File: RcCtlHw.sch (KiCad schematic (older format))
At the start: 27 parts, among them J1 USB_B_Mini, J2 Program, J3 TFT_LCD, SW1 On/Off, U1 TP4056, U2 ESP-M2, U3 ADS1015, U4 Joystick

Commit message: Re-worked USB connector and Joystick to allow oval holes for legs Cleaned up tracks
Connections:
- net at U1.7 (CHRG): now also D1.1 (RA); no longer D1.4 (BA)
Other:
- moved on the sheet: D1
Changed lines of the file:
@@
 F 3 "~" H 4000 2050 50  0001 C CNN
 	1    4000 2100
-	-1   0    0    1
+	-1   0    0    -1
 $EndComp
 Wire Wire Line
@@
 Wire Wire Line
 	3550 2100 3800 2100
-NoConn ~ 3800 2300
 NoConn ~ 2150 1800
 NoConn ~ 2150 1900
@@
 	5250 3750 4750 3750
 Connection ~ 4750 3750
+NoConn ~ 3800 2300
 $EndSCHEMATC

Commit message: More 3D play
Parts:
- D1: footprint LED_THT:LED_D5.0mm-4_RGB -> TrevM:LED_D5.0mm-4_RGB-RIGHT
- J2: footprint Connector_PinHeader_2.54mm:PinHeader_1x06_P2.54mm_Vertical -> TrevM:PinHeader_1x06_P2.54mm_Vertical_bent
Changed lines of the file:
@@
 F 0 "D1" H 4000 1633 50  0000 C CNN
 F 1 "LED_RCGB" H 4000 1724 50  0000 C CNN
-F 2 "LED_THT:LED_D5.0mm-4_RGB" H 4000 2050 50  0001 C CNN
+F 2 "TrevM:LED_D5.0mm-4_RGB-RIGHT" H 4000 2050 50  0001 C CNN
 F 3 "~" H 4000 2050 50  0001 C CNN
 	1    4000 2100
@@
 F 0 "J2" H 8722 1974 50  0000 R CNN
 F 1 "Program" H 8722 1883 50  0000 R CNN
-F 2 "Connector_PinHeader_2.54mm:PinHeader_1x06_P2.54mm_Vertical" H 8750 2000 50  0001 C CNN
+F 2 "TrevM:PinHeader_1x06_P2.54mm_Vertical_bent" H 8750 2000 50  0001 C CNN
 F 3 "~" H 8750 2000 50  0001 C CNN
 	1    8750 2000

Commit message: Added 100n capacitors to ADCs
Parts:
- added C7, C8, C9: 100n, Capacitor_SMD:C_0805_2012Metric, symbol Device:C
- C5, C6: value u1 -> 100n
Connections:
- net GND: now also C7.2, C8.2, C9.2
- net at U3.4 (AIN0), U4.2: now also C7.1
- net at U3.5 (AIN1), U4.5: now also C8.1
- net at R10.1, R9.2, U3.6 (AIN2): now also C9.1
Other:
- moved on the sheet: C5, C6, R8
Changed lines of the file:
@@
 Wire Wire Line
 	7300 5100 7300 5000
-Connection ~ 7650 4300
-Wire Wire Line
-	7650 4600 7650 4300
-Wire Wire Line
-	7650 4900 7650 5000
-Wire Wire Line
-	7300 5000 7650 5000
+Connection ~ 7850 4300
+Wire Wire Line
+	7850 4600 7850 4300
 Wire Wire Line
 	7300 4500 7300 4600
@@
 Text Label 8550 1800 2    39   ~ 0
 3V3
-Connection ~ 7550 1300
+Connection ~ 7650 1300
 Wire Wire Line
 	7950 1800 8550 1800
@@
 	7950 1300 7950 1800
 Wire Wire Line
-	7550 1300 7950 1300
+	7650 1300 7950 1300
 $Comp
 L conn:Conn_01x06_Male J2
@@
 $EndComp
 Wire Wire Line
-	7550 1900 8550 1900
+	7650 1900 8550 1900
 $Comp
 L conn:Conn_01x08_Female J3
@@
 ESP-M2 takes 600 mA max
 Connection ~ 5900 2600
-Wire Wire Line
-	5900 2600 5300 2600
 Connection ~ 8700 3350
 Wire Wire Line
@@
 Wire Wire Line
 	8250 2600 8450 2600
-Wire Wire Line
-	5300 3000 5300 3100
 $Comp
 L TrevM:ADS1015 U3
@@
 $EndComp
 Wire Wire Line
-	7200 4300 7650 4300
+	7200 4300 7850 4300
 $Comp
 L Device:C C6
 U 1 1 60930EB5
-P 7650 4750
-F 0 "C6" H 7765 4796 50  0000 L CNN
-F 1 "u1" H 7765 4705 50  0000 L CNN
-F 2 "Capacitor_SMD:C_0805_2012Metric" H 7688 4600 50  0001 C CNN
-F 3 "~" H 7650 4750 50  0001 C CNN
-	1    7650 4750
+P 7850 4750
+F 0 "C6" H 7850 4850 50  0000 L CNN
+F 1 "100n" H 7850 4650 50  0000 L CNN
+F 2 "Capacitor_SMD:C_0805_2012Metric" H 7888 4600 50  0001 C CNN
+F 3 "~" H 7850 4750 50  0001 C CNN
+	1    7850 4750
 	1    0    0    -1
 $EndComp
@@
 Connection ~ 8250 2600
 $Comp
-L Power:GND #PWR07
-U 1 1 6093378D
-P 5300 3100
-F 0 "#PWR07" H 5300 2850 50  0001 C CNN
-F 1 "GND" H 5305 2927 50  0000 C CNN
-F 2 "" H 5300 3100 50  0001 C CNN
-F 3 "" H 5300 3100 50  0001 C CNN
-	1    5300 3100
-	1    0    0    -1
-$EndComp
-$Comp
 L Power:GND #PWR011
 U 1 1 60932F2B
@@
 L Device:C C5
 U 1 1 6093070F
-P 5300 2850
-F 0 "C5" H 5350 2950 50  0000 L CNN
-F 1 "u1" H 5350 2750 50  0000 L CNN
-F 2 "Capacitor_SMD:C_0805_2012Metric" H 5338 2700 50  0001 C CNN
-F 3 "~" H 5300 2850 50  0001 C CNN
-	1    5300 2850
+P 5900 2850
+F 0 "C5" H 5950 2950 50  0000 L CNN
+F 1 "100n" H 5950 2750 50  0000 L CNN
+F 2 "Capacitor_SMD:C_0805_2012Metric" H 5938 2700 50  0001 C CNN
+F 3 "~" H 5900 2850 50  0001 C CNN
+	1    5900 2850
 	1    0    0    -1
 $EndComp
 Wire Wire Line
 	7350 2500 7550 2500
-Connection ~ 7550 1900
+Connection ~ 7650 1900
 Wire Wire Line
 	7450 2400 8150 2400
@@
 	8150 2400 8150 2000
 Wire Wire Line
-	7550 1900 7350 1900
-Wire Wire Line
-	7550 1700 7550 1900
+	7650 1900 7350 1900
+Wire Wire Line
+	7650 1700 7650 1900
 Connection ~ 7450 1300
 Wire Wire Line
-	7550 1300 7550 1400
-Wire Wire Line
-	7450 1300 7550 1300
+	7650 1300 7650 1400
+Wire Wire Line
+	7450 1300 7650 1300
 $Comp
 L Device:R R8
 U 1 1 6090429E
-P 7550 1550
-F 0 "R8" V 7600 1650 50  0000 L CNN
-F 1 "10K" V 7600 1300 50  0000 L CNN
-F 2 "Resistor_SMD:R_0805_2012Metric" V 7480 1550 50  0001 C CNN
-F 3 "~" H 7550 1550 50  0001 C CNN
-	1    7550 1550
+P 7650 1550
+F 0 "R8" V 7700 1650 50  0000 L CNN
+F 1 "10K" V 7700 1300 50  0000 L CNN
+F 2 "Resistor_SMD:R_0805_2012Metric" V 7580 1550 50  0001 C CNN
+F 3 "~" H 7650 1550 50  0001 C CNN
+	1    7650 1550
 	1    0    0    -1
 $EndComp
@@
 	8350 4000 8350 4300
 Wire Wire Line
-	7650 4300 8350 4300
+	7850 4300 8350 4300
 Connection ~ 8350 4000
 Wire Wire Line
@@
 Connection ~ 6400 4300
 Wire Wire Line
-	7350 2600 7950 2600
+	7350 2600 7450 2600
 NoConn ~ 5950 2300
 Wire Wire Line
@@
 	5700 2100 5950 2100
 Wire Wire Line
-	5300 2700 5300 2600
-Wire Wire Line
-	4850 4200 6300 4200
+	4850 4200 5950 4200
 Wire Wire Line
 	5350 4300 6200 4300
@@
 Connection ~ 4750 3750
 NoConn ~ 3800 2300
+Wire Wire Line
+	7850 5000 7850 4900
+Wire Wire Line
+	7300 5000 7600 5000
+$Comp
+L Device:C C9
+U 1 1 60CFAD69
+P 7600 4750
+F 0 "C9" H 7600 4850 50  0000 L CNN
+F 1 "100n" H 7600 4650 50  0000 L CNN
+F 2 "Capacitor_SMD:C_0805_2012Metric" H 7638 4600 50  0001 C CNN
+F 3 "~" H 7600 4750 50  0001 C CNN
+	1    7600 4750
+	1    0    0    -1
+$EndComp
+Wire Wire Line
+	7300 4500 7600 4500
+Wire Wire Line
+	7600 4500 7600 4600
+Wire Wire Line
+	7600 4900 7600 5000
+Connection ~ 7600 5000
+Wire Wire Line
+	7600 5000 7850 5000
+$Comp
+L Device:C C8
+U 1 1 60D23BED
+P 6200 4750
+F 0 "C8" H 6200 4850 50  0000 L CNN
+F 1 "100n" H 6200 4650 50  0000 L CNN
+F 2 "Capacitor_SMD:C_0805_2012Metric" H 6238 4600 50  0001 C CNN
+F 3 "~" H 6200 4750 50  0001 C CNN
+	1    6200 4750
+	1    0    0    -1
+$EndComp
+$Comp
+L Device:C C7
+U 1 1 60D247AF
+P 5950 4750
+F 0 "C7" H 5950 4850 50  0000 L CNN
+F 1 "100n" H 5950 4650 50  0000 L CNN
+F 2 "Capacitor_SMD:C_0805_2012Metric" H 5988 4600 50  0001 C CNN
+F 3 "~" H 5950 4750 50  0001 C CNN
+	1    5950 4750
+	1    0    0    -1
+$EndComp
+Wire Wire Line
+	6400 5000 6200 5000
+Connection ~ 6400 5000
+Wire Wire Line
+	6200 4900 6200 5000
+Connection ~ 6200 5000
+Wire Wire Line
+	6200 4600 6200 4500
+Connection ~ 6200 4500
+Wire Wire Line
+	5950 4600 5950 4200
+Connection ~ 5950 4200
+Wire Wire Line
+	5950 4200 6300 4200
+Wire Wire Line
+	5950 5000 5950 4900
+Wire Wire Line
+	5950 5000 6200 5000
+Wire Wire Line
+	5900 2700 5900 2600
+Wire Wire Line
+	7450 2600 7450 3050
+Wire Wire Line
+	7450 3050 5900 3050
+Wire Wire Line
+	5900 3050 5900 3000
+Connection ~ 7450 2600
+Wire Wire Line
+	7450 2600 7950 2600
 $EndSCHEMATC

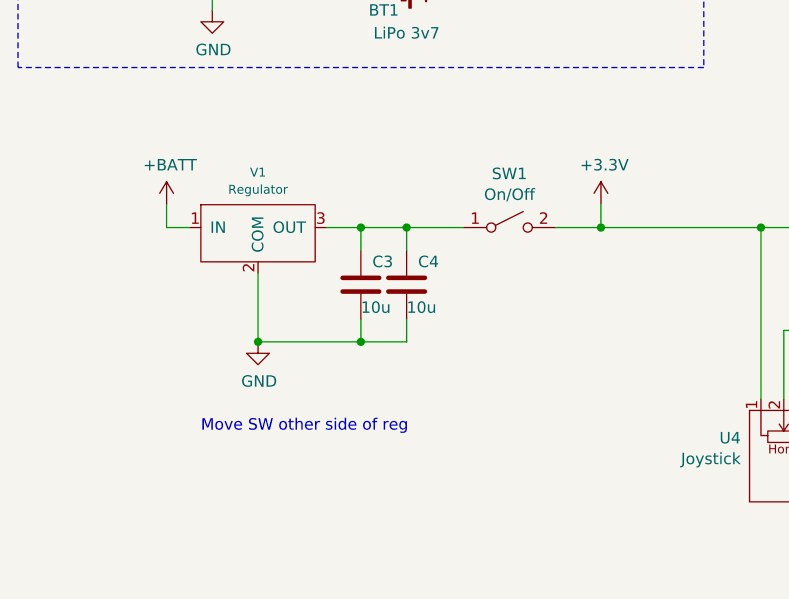
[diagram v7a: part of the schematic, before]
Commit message: Move switch to before regulator
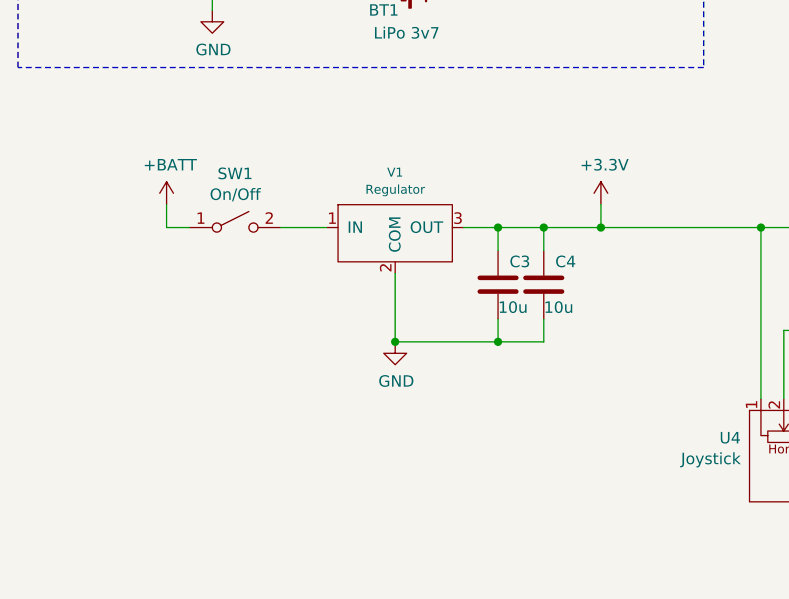
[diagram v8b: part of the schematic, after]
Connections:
- net +3V3: now also C3.1, C4.1, V1.3 (OUT); no longer SW1.2 (B)
- net +BATT: now also SW1.1 (A); no longer V1.1 (IN)
- new net: SW1.2 (B), V1.1 (IN)
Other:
- note removed: "Move SW other side of reg"
- moved on the sheet: C3, C4, SW1, V1
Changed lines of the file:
@@
 L TrevM:Regulator V1
 U 1 1 60B161BB
-P 2550 3650
-F 0 "V1" H 2550 3791 39  0000 C CNN
-F 1 "Regulator" H 2550 3716 39  0000 C CNN
-F 2 "Package_TO_SOT_SMD:TO-252-2" H 2550 3650 39  0001 C CNN
-F 3 "" H 2550 3650 39  0001 C CNN
-	1    2550 3650
+P 3150 3650
+F 0 "V1" H 3150 3791 39  0000 C CNN
+F 1 "Regulator" H 3150 3716 39  0000 C CNN
+F 2 "Package_TO_SOT_SMD:TO-252-2" H 3150 3650 39  0001 C CNN
+F 3 "" H 3150 3650 39  0001 C CNN
+	1    3150 3650
 	1    0    0    -1
 $EndComp
 Wire Wire Line
 	2150 3650 2150 3750
-Wire Wire Line
-	2150 3750 2250 3750
 $Comp
 L switches:SW_SPST SW1
 U 1 1 60B1FF41
-P 3650 3750
-F 0 "SW1" H 3650 3985 50  0000 C CNN
-F 1 "On/Off" H 3650 3894 50  0000 C CNN
-F 2 "TrevM:SlideSwitch" H 3650 3750 50  0001 C CNN
-F 3 "~" H 3650 3750 50  0001 C CNN
-	1    3650 3750
+P 2450 3750
+F 0 "SW1" H 2450 3985 50  0000 C CNN
+F 1 "On/Off" H 2450 3894 50  0000 C CNN
+F 2 "TrevM:SlideSwitch" H 2450 3750 50  0001 C CNN
+F 3 "~" H 2450 3750 50  0001 C CNN
+	1    2450 3750
 	1    0    0    -1
 $EndComp
@@
 $EndComp
 Wire Wire Line
-	3850 3750 4050 3750
-Wire Wire Line
 	4050 3750 4050 3650
 $Comp
@@
 L Power:GND #PWR03
 U 1 1 60B3B029
-P 2550 4250
-F 0 "#PWR03" H 2550 4000 50  0001 C CNN
-F 1 "GND" H 2555 4077 50  0000 C CNN
-F 2 "" H 2550 4250 50  0001 C CNN
-F 3 "" H 2550 4250 50  0001 C CNN
-	1    2550 4250
+P 3150 4250
+F 0 "#PWR03" H 3150 4000 50  0001 C CNN
+F 1 "GND" H 3155 4077 50  0000 C CNN
+F 2 "" H 3150 4250 50  0001 C CNN
+F 3 "" H 3150 4250 50  0001 C CNN
+	1    3150 4250
 	1    0    0    -1
 $EndComp
@@
 L Device:C C3
 U 1 1 60B94DB4
-P 3000 4000
-F 0 "C3" H 3050 4100 50  0000 L CNN
-F 1 "10u" H 3000 3900 50  0000 L CNN
-F 2 "Capacitor_SMD:C_0805_2012Metric" H 3038 3850 50  0001 C CNN
-F 3 "~" H 3000 4000 50  0001 C CNN
-	1    3000 4000
+P 3600 4000
+F 0 "C3" H 3650 4100 50  0000 L CNN
+F 1 "10u" H 3600 3900 50  0000 L CNN
+F 2 "Capacitor_SMD:C_0805_2012Metric" H 3638 3850 50  0001 C CNN
+F 3 "~" H 3600 4000 50  0001 C CNN
+	1    3600 4000
 	1    0    0    -1
 $EndComp
@@
 L Device:C C4
 U 1 1 60B957EB
-P 3200 4000
-F 0 "C4" H 3250 4100 50  0000 L CNN
-F 1 "10u" H 3200 3900 50  0000 L CNN
-F 2 "Capacitor_SMD:C_0805_2012Metric" H 3238 3850 50  0001 C CNN
-F 3 "~" H 3200 4000 50  0001 C CNN
-	1    3200 4000
-	1    0    0    -1
-$EndComp
-Wire Wire Line
-	2850 3750 3000 3750
-Wire Wire Line
-	3000 3850 3000 3750
-Connection ~ 3000 3750
-Wire Wire Line
-	3000 3750 3200 3750
-Wire Wire Line
-	3200 3850 3200 3750
-Wire Wire Line
-	2550 3950 2550 4250
-Wire Wire Line
-	2550 4250 3000 4250
-Wire Wire Line
-	3200 4250 3200 4150
-Connection ~ 2550 4250
-Wire Wire Line
-	3000 4150 3000 4250
-Connection ~ 3000 4250
-Wire Wire Line
-	3000 4250 3200 4250
-Wire Wire Line
-	3450 3750 3200 3750
-Connection ~ 3200 3750
+P 3800 4000
+F 0 "C4" H 3850 4100 50  0000 L CNN
+F 1 "10u" H 3800 3900 50  0000 L CNN
+F 2 "Capacitor_SMD:C_0805_2012Metric" H 3838 3850 50  0001 C CNN
+F 3 "~" H 3800 4000 50  0001 C CNN
+	1    3800 4000
+	1    0    0    -1
+$EndComp
+Wire Wire Line
+	3450 3750 3600 3750
+Wire Wire Line
+	3600 3850 3600 3750
+Connection ~ 3600 3750
+Wire Wire Line
+	3600 3750 3800 3750
+Wire Wire Line
+	3800 3850 3800 3750
+Wire Wire Line
+	3150 3950 3150 4250
+Wire Wire Line
+	3150 4250 3600 4250
+Wire Wire Line
+	3800 4250 3800 4150
+Connection ~ 3150 4250
+Wire Wire Line
+	3600 4150 3600 4250
+Connection ~ 3600 4250
+Wire Wire Line
+	3600 4250 3800 4250
+Connection ~ 3800 3750
 $Comp
 L Power:+BATT #PWR0101
@@
 	1    0    0    -1
 $EndComp
-Text Notes 2300 4650 0    50   ~ 0
-Move SW other side of reg
 $Comp
 L TrevM:LDO_2V8 V2
@@
 Wire Wire Line
 	7450 2600 7950 2600
+Wire Wire Line
+	3800 3750 4050 3750
+Wire Wire Line
+	2650 3750 2850 3750
+Wire Wire Line
+	2250 3750 2150 3750
 $EndSCHEMATC
